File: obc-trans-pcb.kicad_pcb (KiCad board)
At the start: 2 copper layers, 96 x 90 mm, 30 parts, among them IC1 DS3234, J1 H1, J2 H2, J3 H_EPS, J4 DEBUGGING PORT, J5 PROGRAMMING PORT, SW1 SW_RST, U1 SN65HVD230, U2 ATMEGA32M1-MU, U3 SST25VF016B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

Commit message: finished layout
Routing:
- net GND: track 88.1 -> 94.1 mm, vias 22 -> 23
- net +3V3: track 78.0 -> 81.2 mm, vias 16 -> 17
- added copper zone on In2.Cu, net +3V3
- added copper zone on In1.Cu, net GND
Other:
- copper layers 2 -> 4

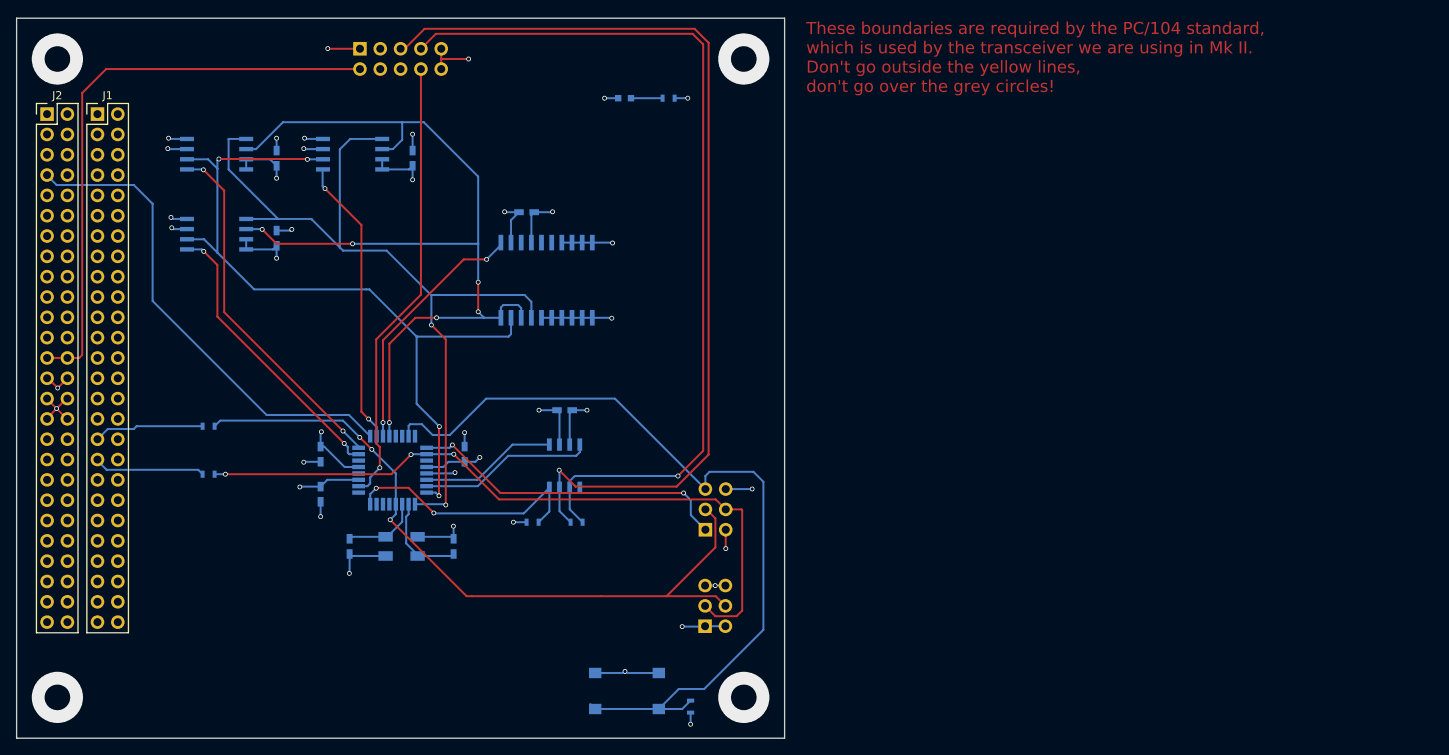
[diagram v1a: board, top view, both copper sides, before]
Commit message: corrected some pads, caps, & vias
fixed vias too close together, corrected via clearance, fixed some caps wired incorrectly (I think), renamed inner layers for clarity. Also connected a pad I missed
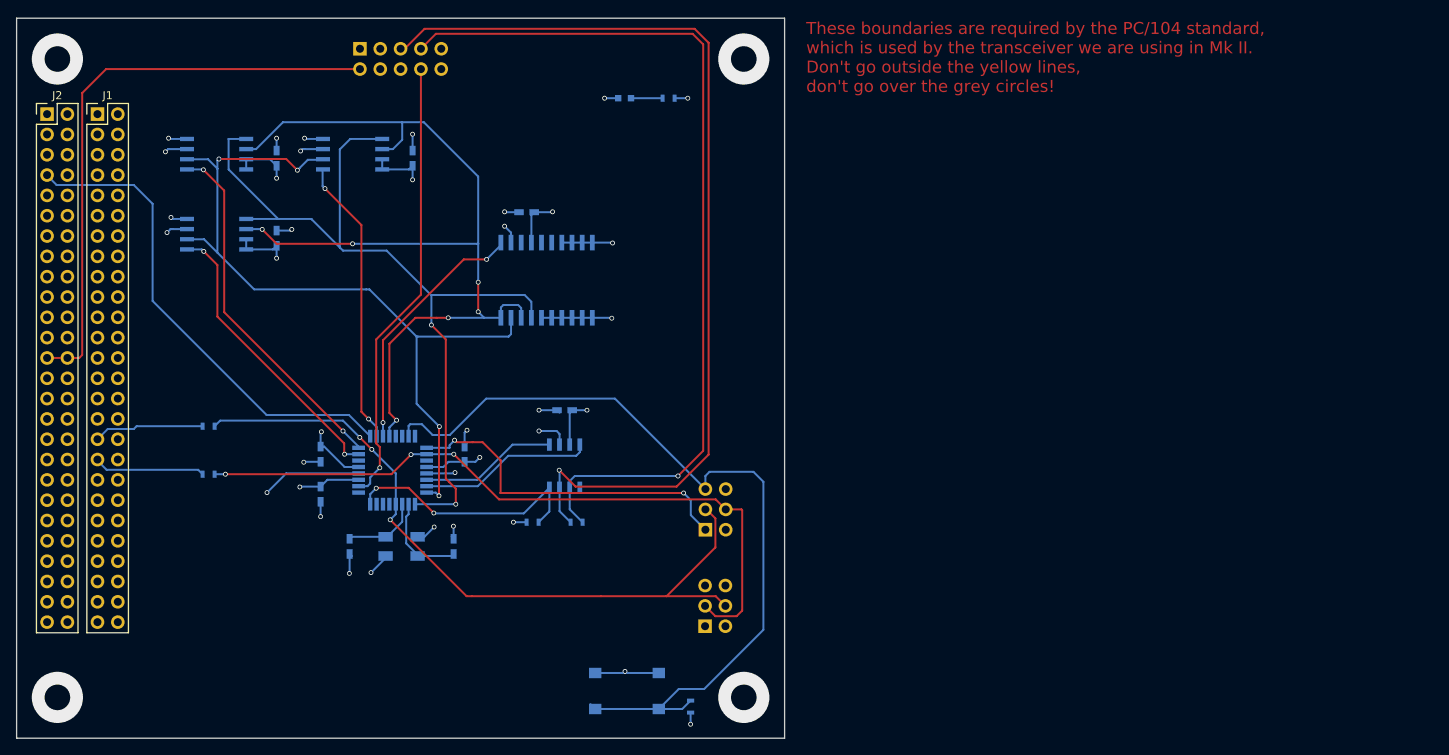
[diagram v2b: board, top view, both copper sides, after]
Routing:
- net +3V3: track 81.2 -> 67.4 mm, vias 17 -> 13
- net GND: track 94.1 -> 83.0 mm, vias 23 -> 24
- net /MISO_A: track 40.5 -> 43.6 mm
- net /MOSI: track 105.7 -> 107.3 mm
- net /MISO: track 99.6 -> 100.9 mm
- net /SCK: track 118.5 -> 119.2 mm
- added copper zone on 3V3-In2.Cu, net +3V3
- added copper zone on GND-In1.Cu, net GND
- removed copper zone on In2.Cu, net +3V3
- removed copper zone on In1.Cu, net GND

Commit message: fixed corner locations, header location, pours
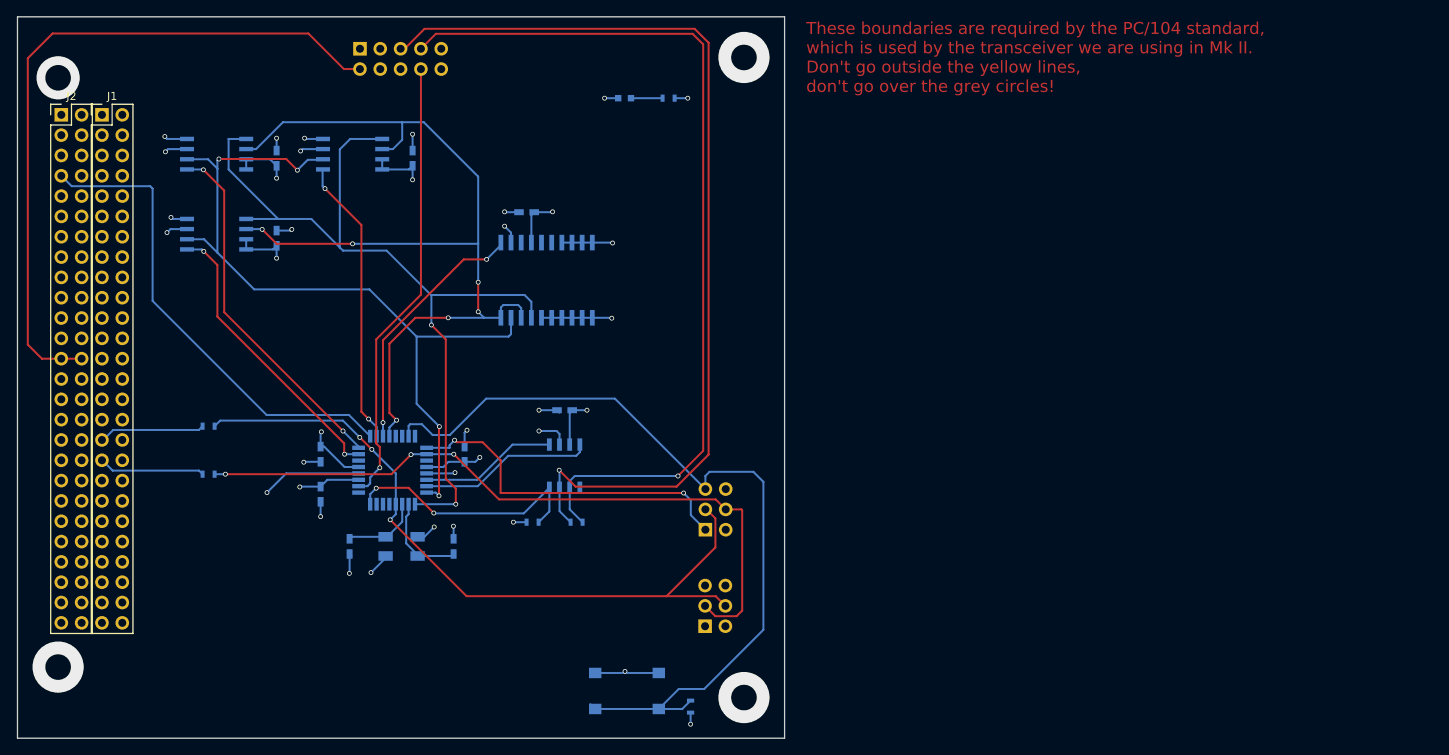
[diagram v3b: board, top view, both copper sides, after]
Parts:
- moved J2 1.78 mm to (105.6, 62.1)
- moved J1 0.57 mm to (110.7, 62.1)
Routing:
- net +5V: track 73.3 -> 87.9 mm
- net /EN_UHF: track 61.1 -> 60.3 mm
- net /COM_TXD: track 14.0 -> 13.3 mm
- net /COM_RXD: track 13.8 -> 13.3 mm
- net GND: track 83.0 -> 83.2 mm, vias 24 -> 28
- net (no net): vias 4 -> 0
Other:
- board size 96 x 90 mm -> 95.9 x 90.2 mm

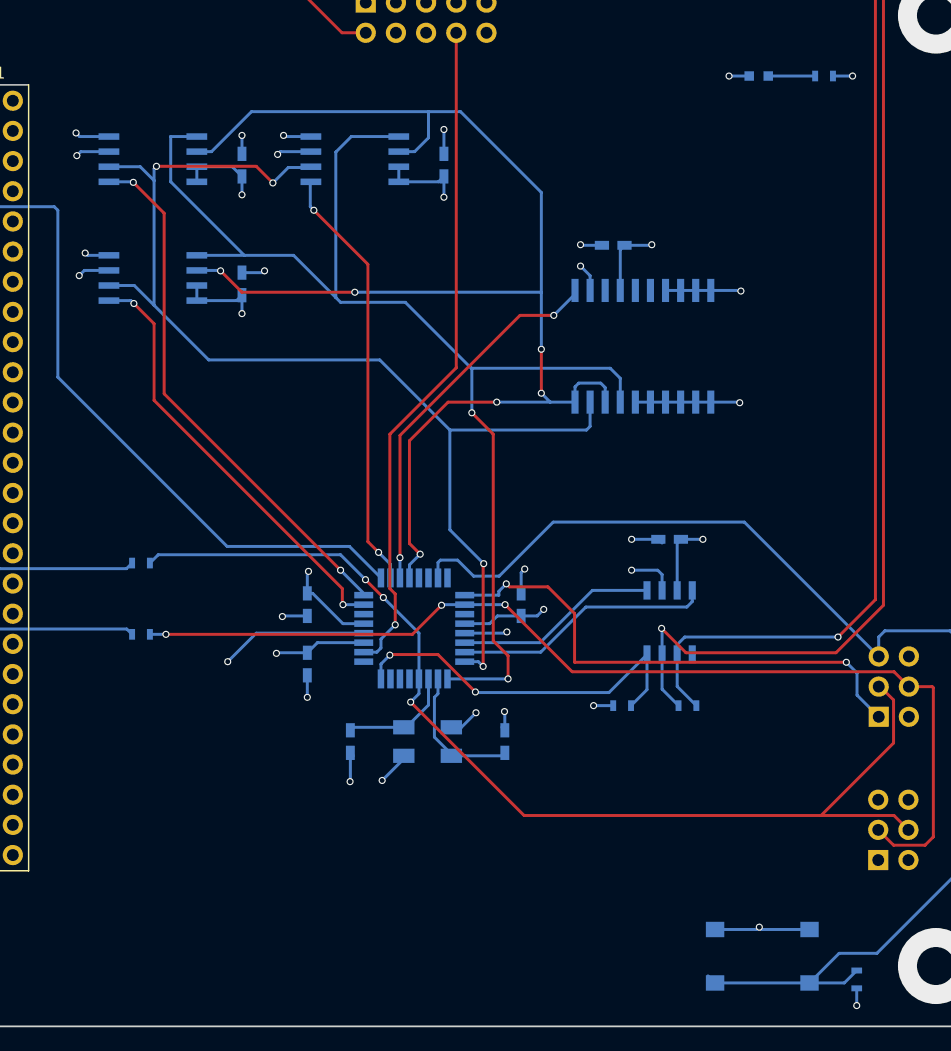
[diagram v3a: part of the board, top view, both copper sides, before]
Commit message: .8 mm vias + logo
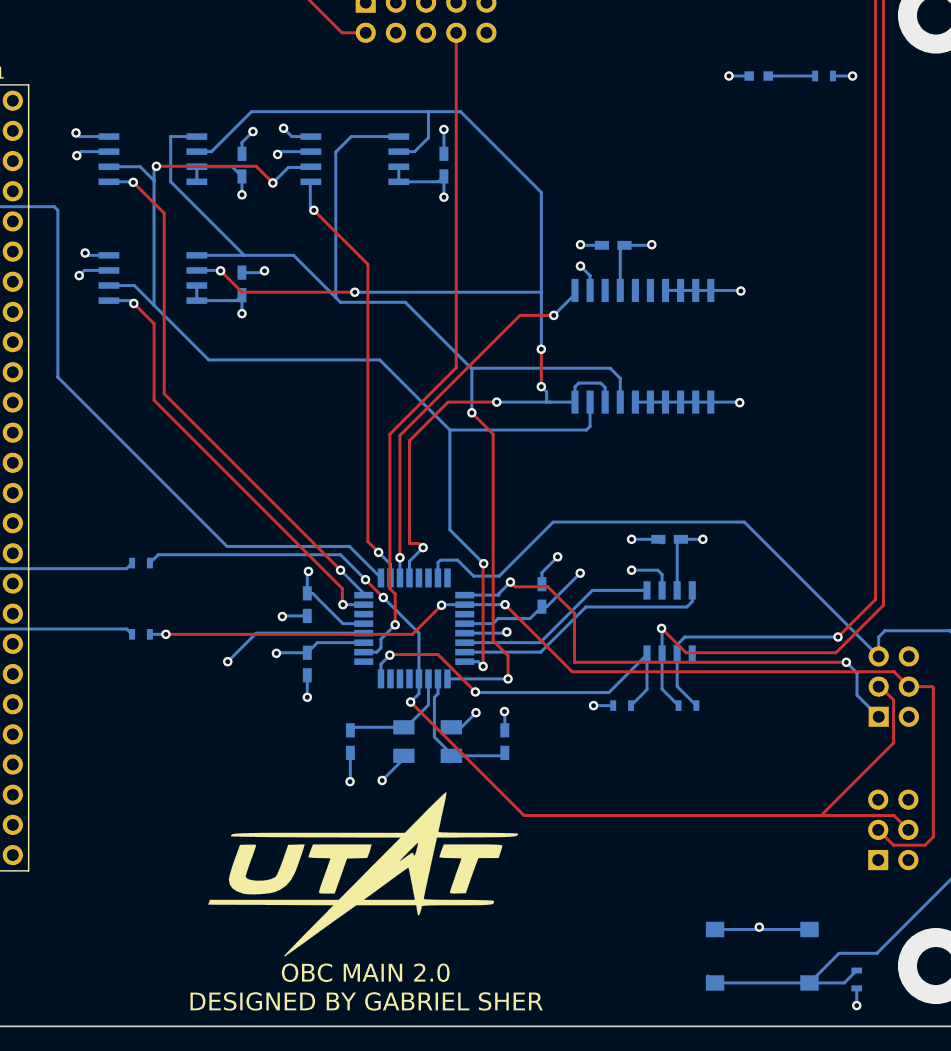
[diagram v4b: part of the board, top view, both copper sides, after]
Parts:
- added G***: LOGO, obc-trans-pcb:utat-logo, F.Cu at (142.8, 126.8)
- moved C2 1.91 mm to (157.8, 103.7)
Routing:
- net +3V3: track 67.4 -> 71.7 mm
- net GND: track 83.2 -> 85.0 mm
- net /SCK: track 119.0 -> 119.6 mm
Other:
- board text added: "OBC MAIN 2.0 DESIGNED BY GABRIEL SHER"

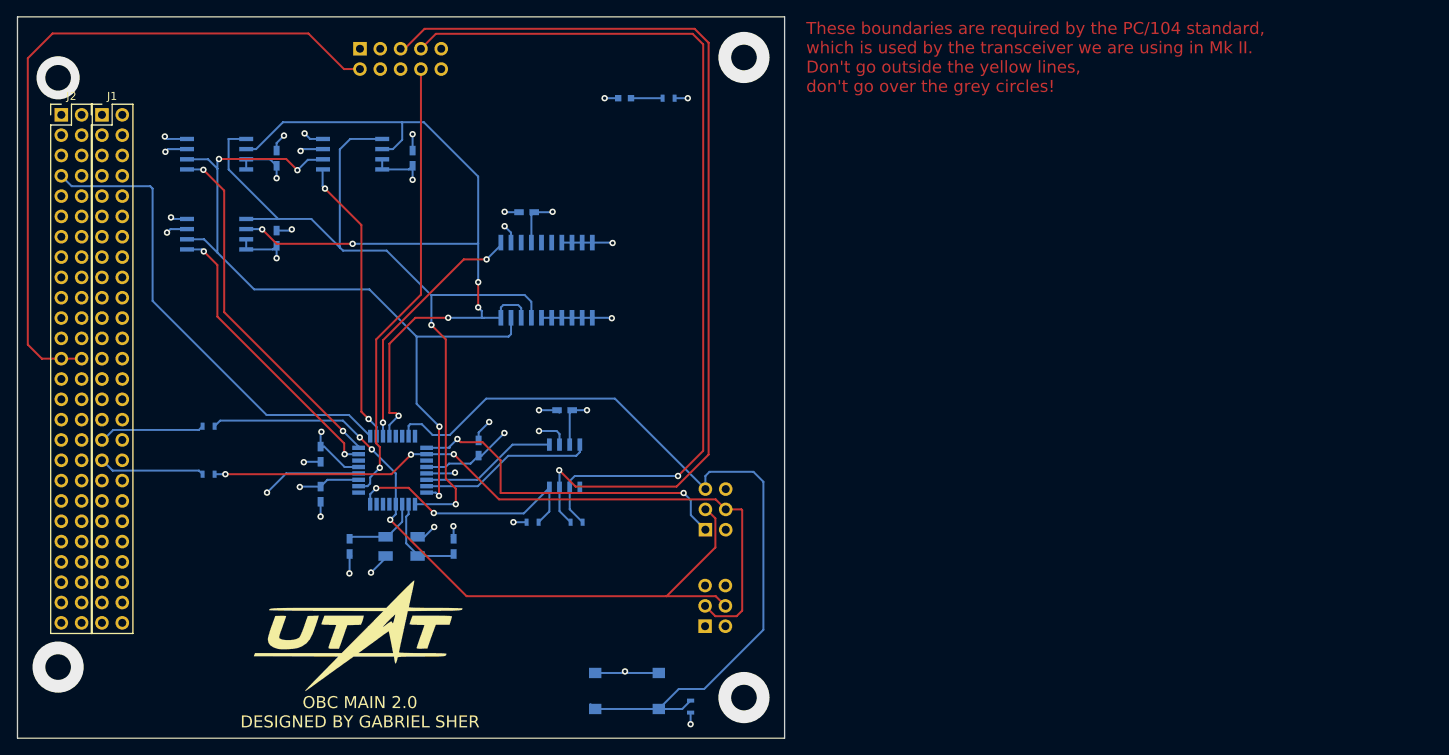
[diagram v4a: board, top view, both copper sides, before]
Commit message: finished 1.2 holes and drawings
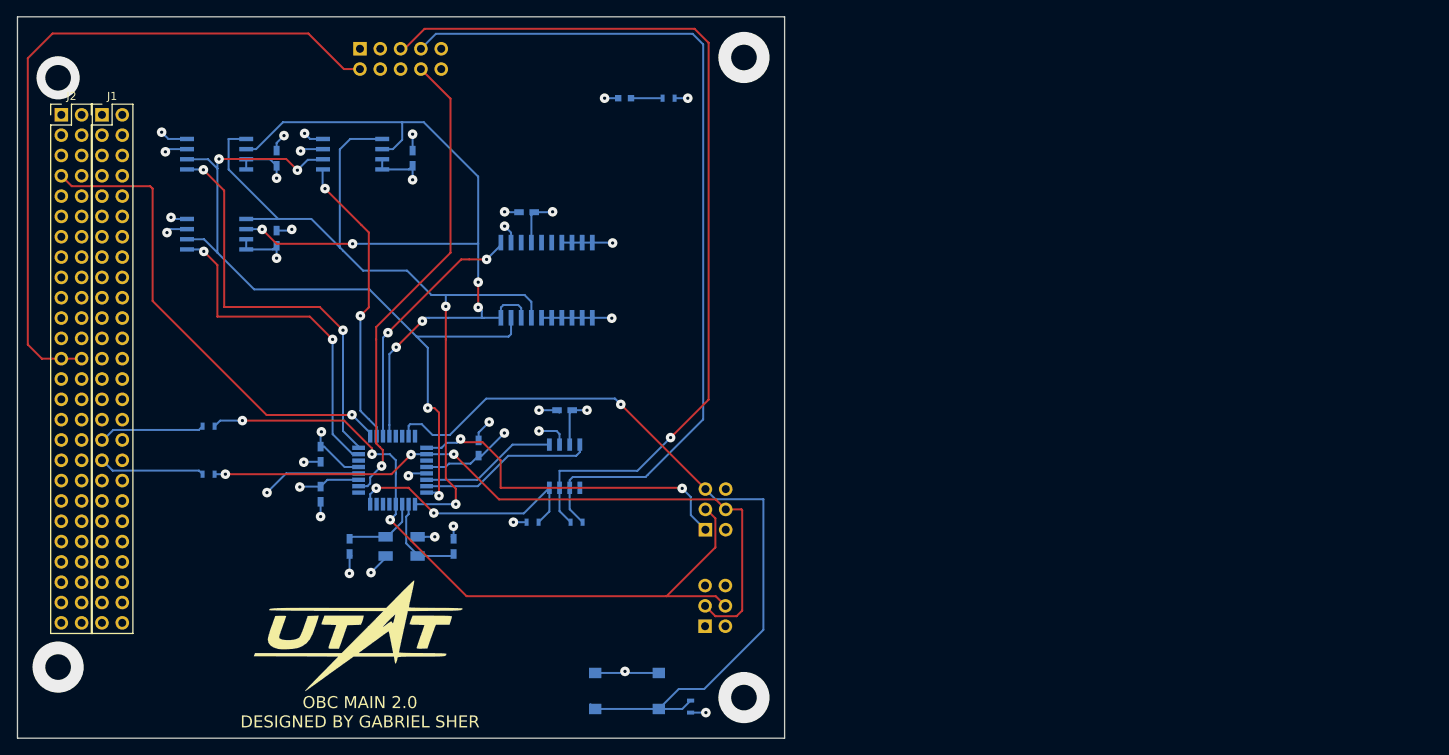
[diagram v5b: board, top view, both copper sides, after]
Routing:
- net /CS_MEM2: track 44.9 -> 51.9 mm
- net /CS_MEM3: track 36.6 -> 42.8 mm
- net /CANH: track 120.1 -> 114.2 mm
- net /RST: track 104.1 -> 100.1 mm, vias 0 -> 1
- net /EPS_RST: track 56.4 -> 59.8 mm
- net /CANL: track 111.5 -> 109.2 mm, vias 1 -> 0
- net /SCK: track 119.6 -> 117.4 mm
- net /SCK_A: track 92.1 -> 93.5 mm
- net /CS_MEM1: track 36.2 -> 37.0 mm
- net /MOSI: track 107.3 -> 106.6 mm
- net /EN_UHF: track 60.3 -> 60.6 mm, vias 0 -> 1
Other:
- board text removed: "These boundaries are required by the PC/104 standard, which is used by the transceiver we are using in Mk II. Don't go outside the yellow lines, don't go over the grey circles!"
